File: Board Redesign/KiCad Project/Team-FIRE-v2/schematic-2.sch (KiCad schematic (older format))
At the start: 20 parts, among them J3 USB_B_Mini, J4 Conn_01x03, J5 Conn_ARM_JTAG_SWD_10, U4 TXB0108DQSR, U7 TXB0104RUT

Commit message: Fix: connection of IO-RI
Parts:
- renumbered D2 to D?, D3 to D?, D4 to D?, D5 to D?, J5 to J?, J3 to J?, R11 to R?, R13 to R?, R15 to R?, R16 to R?
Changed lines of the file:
@@
 uC Support
 $Comp
-L Connector:Conn_ARM_JTAG_SWD_10 J5
+L Connector:Conn_ARM_JTAG_SWD_10 J?
 U 1 1 5E6DB242
 P 6220 3020
@@
 $EndComp
 $Comp
-L power:+3.3V #PWR0125
+L power:+3.3V #PWR?
 U 1 1 5E6DD1DD
 P 6970 2770
@@
 	6970 3020 6820 3020
 $Comp
-L power:GND #PWR0126
+L power:GND #PWR?
 U 1 1 5E6E026F
 P 5520 3270
@@
 Keep reset button?
 $Comp
-L Connector:USB_B_Mini J3
+L Connector:USB_B_Mini J?
 U 1 1 5E6EF352
 P 4470 2920
@@
 $EndComp
 $Comp
-L power:GND #PWR0127
+L power:GND #PWR?
 U 1 1 5E6F0DA3
 P 4370 3570
@@
 	5070 3020 4770 3020
 $Comp
-L Device:LED_Small D2
+L Device:LED_Small D?
 U 1 1 5E707545
 P 7670 2920
@@
 $EndComp
 $Comp
-L Device:LED_Small D3
+L Device:LED_Small D?
 U 1 1 5E7081BA
 P 8170 2920
@@
 $EndComp
 $Comp
-L Device:LED_Small D4
+L Device:LED_Small D?
 U 1 1 5E7085D2
 P 8670 3270
@@
 $EndComp
 $Comp
-L Device:LED_Small D5
+L Device:LED_Small D?
 U 1 1 5E709852
 P 9170 3270
@@
 $EndComp
 $Comp
-L power:+3.3V #PWR0128
+L power:+3.3V #PWR?
 U 1 1 5E709BE1
 P 8670 2670
@@
 $EndComp
 $Comp
-L power:+3.3V #PWR0129
+L power:+3.3V #PWR?
 U 1 1 5E70A194
 P 9170 2670
@@
 $EndComp
 $Comp
-L power:GND #PWR0130
+L power:GND #PWR?
 U 1 1 5E70A4EC
 P 7670 2670
@@
 $EndComp
 $Comp
-L power:GND #PWR0131
+L power:GND #PWR?
 U 1 1 5E70B5A5
 P 8170 2670
@@
 $EndComp
 $Comp
-L Device:R R11
+L Device:R R?
 U 1 1 5E70B7B8
 P 7670 3320
@@
 $EndComp
 $Comp
-L Device:R R13
+L Device:R R?
 U 1 1 5E70C353
 P 8170 3320
@@
 $EndComp
 $Comp
-L Device:R R15
+L Device:R R?
 U 1 1 5E7177B2
 P 8670 2920
@@
 $EndComp
 $Comp
-L Device:R R16
+L Device:R R?
 U 1 1 5E717AD1
 P 9170 2920

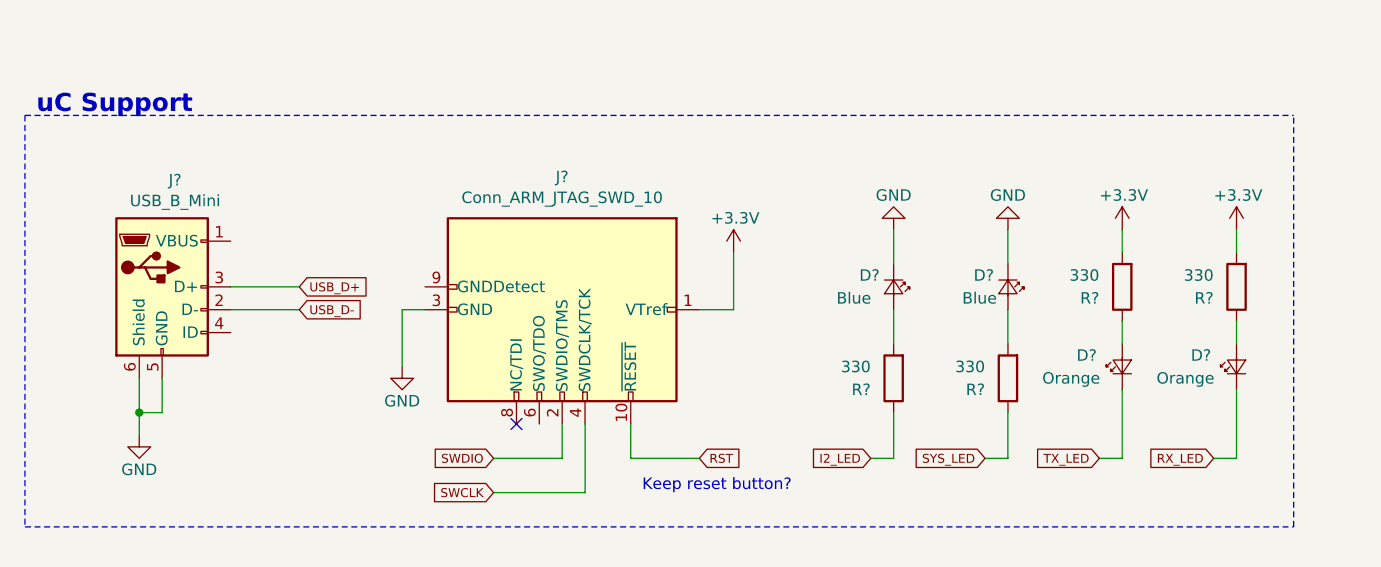
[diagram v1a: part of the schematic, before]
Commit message: Starting complete BOM generation
- Finished schematic(s)
- Started BOM information assignment for final BOM sent to NASA
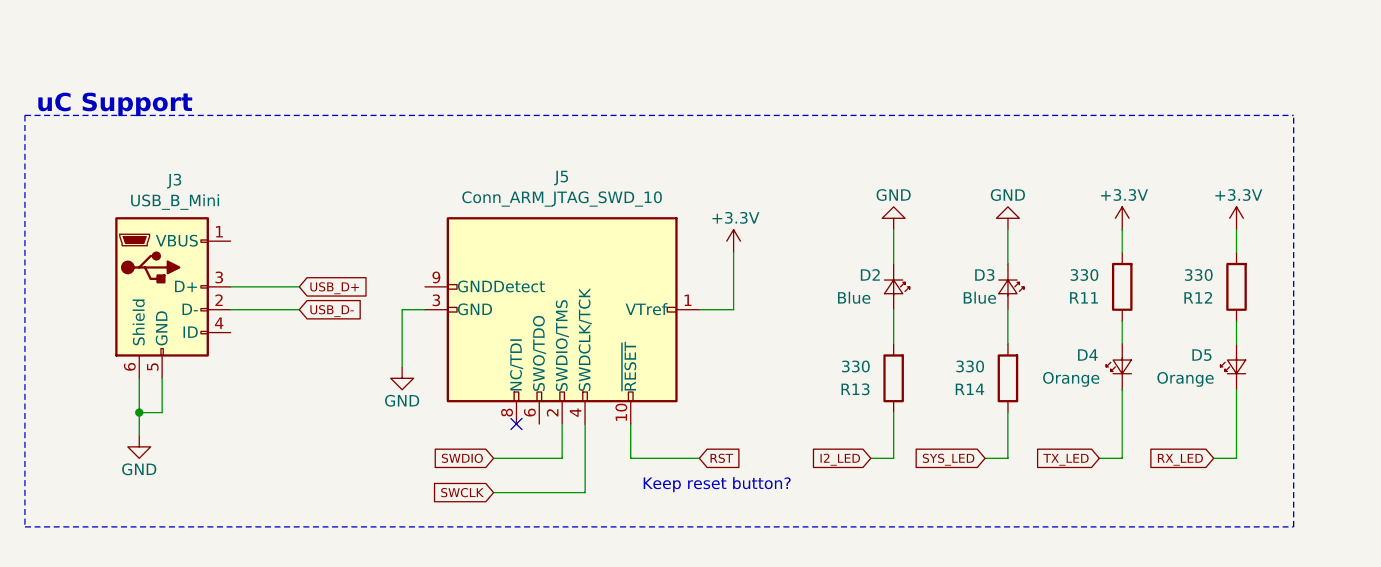
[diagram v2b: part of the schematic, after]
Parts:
- gave numbers to parts that had none: 10
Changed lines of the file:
@@
 EESchema Schematic File Version 4
+LIBS:Team-FIRE-v2-cache
 EELAYER 30 0
 EELAYER END
@@
 Text Notes 3920 2170 0    79   ~ 16
 uC Support
-$Comp
-L Connector:Conn_ARM_JTAG_SWD_10 J?
-U 1 1 5E6DB242
-P 6220 3020
-F 0 "J?" V 5639 3020 50  0000 C CNN
-F 1 "Conn_ARM_JTAG_SWD_10" V 5730 3020 50  0000 C CNN
-F 2 "" H 6220 3020 50  0001 C CNN
-F 3 "http://infocenter.arm.com/help/topic/com.arm.doc.ddi0314h/DDI0314H_coresight_components_trm.pdf" V 5870 1770 50  0001 C CNN
-	1    6220 3020
-	0    1    1    0
-$EndComp
-$Comp
-L power:+3.3V #PWR?
-U 1 1 5E6DD1DD
-P 6970 2770
-F 0 "#PWR?" H 6970 2620 50  0001 C CNN
-F 1 "+3.3V" H 6870 2920 50  0000 L CNN
-F 2 "" H 6970 2770 50  0001 C CNN
-F 3 "" H 6970 2770 50  0001 C CNN
-	1    6970 2770
-	1    0    0    -1
-$EndComp
-Wire Wire Line
-	6970 2770 6970 3020
-Wire Wire Line
-	6970 3020 6820 3020
-$Comp
-L power:GND #PWR?
-U 1 1 5E6E026F
-P 5520 3270
-F 0 "#PWR?" H 5520 3020 50  0001 C CNN
-F 1 "GND" H 5520 3120 50  0000 C CNN
-F 2 "" H 5520 3270 50  0001 C CNN
-F 3 "" H 5520 3270 50  0001 C CNN
-	1    5520 3270
-	1    0    0    -1
-$EndComp
-Wire Wire Line
-	5620 3020 5520 3020
-Wire Wire Line
-	5520 3020 5520 3270
 Text GLabel 5920 3670 0    39   Input ~ 0
 SWDIO
@@
 Keep reset button?
 $Comp
-L Connector:USB_B_Mini J?
+L Connector:USB_B_Mini J3
 U 1 1 5E6EF352
 P 4470 2920
-F 0 "J?" H 4527 3387 50  0000 C CNN
+F 0 "J3" H 4527 3387 50  0000 C CNN
 F 1 "USB_B_Mini" H 4527 3296 50  0000 C CNN
 F 2 "" H 4620 2870 50  0001 C CNN
@@
 $EndComp
 $Comp
-L power:GND #PWR?
+L power:GND #PWR0127
 U 1 1 5E6F0DA3
 P 4370 3570
-F 0 "#PWR?" H 4370 3320 50  0001 C CNN
+F 0 "#PWR0127" H 4370 3320 50  0001 C CNN
 F 1 "GND" H 4370 3420 50  0000 C CNN
 F 2 "" H 4370 3570 50  0001 C CNN
@@
 	5070 3020 4770 3020
 $Comp
-L Device:LED_Small D?
+L Device:LED_Small D2
 U 1 1 5E707545
 P 7670 2920
-F 0 "D?" V 7620 2770 50  0000 L CNN
+F 0 "D2" V 7620 2770 50  0000 L CNN
 F 1 "Blue" V 7720 2670 50  0000 L CNN
 F 2 "" V 7670 2920 50  0001 C CNN
@@
 $EndComp
 $Comp
-L Device:LED_Small D?
+L Device:LED_Small D3
 U 1 1 5E7081BA
 P 8170 2920
-F 0 "D?" V 8120 2770 50  0000 L CNN
+F 0 "D3" V 8120 2770 50  0000 L CNN
 F 1 "Blue" V 8220 2720 50  0000 L CNN
 F 2 "" V 8170 2920 50  0001 C CNN
@@
 $EndComp
 $Comp
-L Device:LED_Small D?
+L Device:LED_Small D4
 U 1 1 5E7085D2
 P 8670 3270
-F 0 "D?" V 8720 3470 50  0000 R CNN
+F 0 "D4" V 8720 3470 50  0000 R CNN
 F 1 "Orange" V 8620 3620 50  0000 R CNN
 F 2 "" V 8670 3270 50  0001 C CNN
@@
 $EndComp
 $Comp
-L Device:LED_Small D?
+L Device:LED_Small D5
 U 1 1 5E709852
 P 9170 3270
-F 0 "D?" V 9220 3470 50  0000 R CNN
+F 0 "D5" V 9220 3470 50  0000 R CNN
 F 1 "Orange" V 9120 3620 50  0000 R CNN
 F 2 "" V 9170 3270 50  0001 C CNN
@@
 $EndComp
 $Comp
-L power:+3.3V #PWR?
+L power:+3.3V #PWR0128
 U 1 1 5E709BE1
 P 8670 2670
-F 0 "#PWR?" H 8670 2520 50  0001 C CNN
+F 0 "#PWR0128" H 8670 2520 50  0001 C CNN
 F 1 "+3.3V" H 8570 2820 50  0000 L CNN
 F 2 "" H 8670 2670 50  0001 C CNN
@@
 $EndComp
 $Comp
-L power:+3.3V #PWR?
+L power:+3.3V #PWR0129
 U 1 1 5E70A194
 P 9170 2670
-F 0 "#PWR?" H 9170 2520 50  0001 C CNN
+F 0 "#PWR0129" H 9170 2520 50  0001 C CNN
 F 1 "+3.3V" H 9070 2820 50  0000 L CNN
 F 2 "" H 9170 2670 50  0001 C CNN
@@
 $EndComp
 $Comp
-L power:GND #PWR?
+L power:GND #PWR0130
 U 1 1 5E70A4EC
 P 7670 2670
-F 0 "#PWR?" H 7670 2420 50  0001 C CNN
+F 0 "#PWR0130" H 7670 2420 50  0001 C CNN
 F 1 "GND" H 7670 2520 50  0000 C CNN
 F 2 "" H 7670 2670 50  0001 C CNN
@@
 $EndComp
 $Comp
-L power:GND #PWR?
+L power:GND #PWR0131
 U 1 1 5E70B5A5
 P 8170 2670
-F 0 "#PWR?" H 8170 2420 50  0001 C CNN
+F 0 "#PWR0131" H 8170 2420 50  0001 C CNN
 F 1 "GND" H 8170 2520 50  0000 C CNN
 F 2 "" H 8170 2670 50  0001 C CNN
@@
 $EndComp
 $Comp
-L Device:R R?
+L Device:R R13
 U 1 1 5E70B7B8
 P 7670 3320
-F 0 "R?" H 7770 3370 50  0000 L CNN
+F 0 "R13" H 7770 3370 50  0000 L CNN
 F 1 "330" H 7770 3270 50  0000 L CNN
 F 2 "Resistor_SMD:R_0603_1608Metric" V 7600 3320 50  0001 C CNN
@@
 $EndComp
 $Comp
-L Device:R R?
+L Device:R R14
 U 1 1 5E70C353
 P 8170 3320
-F 0 "R?" H 8270 3370 50  0000 L CNN
+F 0 "R14" H 8270 3370 50  0000 L CNN
 F 1 "330" H 8270 3270 50  0000 L CNN
 F 2 "Resistor_SMD:R_0603_1608Metric" V 8100 3320 50  0001 C CNN
@@
 $EndComp
 $Comp
-L Device:R R?
+L Device:R R11
 U 1 1 5E7177B2
 P 8670 2920
-F 0 "R?" H 8770 2970 50  0000 L CNN
+F 0 "R11" H 8770 2970 50  0000 L CNN
 F 1 "330" H 8770 2870 50  0000 L CNN
 F 2 "Resistor_SMD:R_0603_1608Metric" V 8600 2920 50  0001 C CNN
@@
 $EndComp
 $Comp
-L Device:R R?
+L Device:R R12
 U 1 1 5E717AD1
 P 9170 2920
-F 0 "R?" H 9270 2970 50  0000 L CNN
+F 0 "R12" H 9270 2970 50  0000 L CNN
 F 1 "330" H 9270 2870 50  0000 L CNN
 F 2 "Resistor_SMD:R_0603_1608Metric" V 9100 2920 50  0001 C CNN
@@
 F1 "SAMD51_IO.sch" 50
 $EndSheet
+Wire Wire Line
+	6970 3020 6820 3020
+Wire Wire Line
+	6970 2770 6970 3020
+$Comp
+L power:+3.3V #PWR0132
+U 1 1 5E6DD1DD
+P 6970 2770
+F 0 "#PWR0132" H 6970 2620 50  0001 C CNN
+F 1 "+3.3V" H 6870 2920 50  0000 L CNN
+F 2 "" H 6970 2770 50  0001 C CNN
+F 3 "" H 6970 2770 50  0001 C CNN
+	1    6970 2770
+	1    0    0    -1
+$EndComp
+$Comp
+L Connector:Conn_ARM_JTAG_SWD_10 J5
+U 1 1 5E6DB242
+P 6220 3020
+F 0 "J5" V 5639 3020 50  0000 C CNN
+F 1 "Conn_ARM_JTAG_SWD_10" V 5730 3020 50  0000 C CNN
+F 2 "" H 6220 3020 50  0001 C CNN
+F 3 "http://infocenter.arm.com/help/topic/com.arm.doc.ddi0314h/DDI0314H_coresight_components_trm.pdf" V 5870 1770 50  0001 C CNN
+	1    6220 3020
+	0    1    1    0
+$EndComp
+Wire Wire Line
+	5520 3020 5520 3270
+Wire Wire Line
+	5620 3020 5520 3020
+$Comp
+L power:GND #PWR0133
+U 1 1 5E6E026F
+P 5520 3270
+F 0 "#PWR0133" H 5520 3020 50  0001 C CNN
+F 1 "GND" H 5520 3120 50  0000 C CNN
+F 2 "" H 5520 3270 50  0001 C CNN
+F 3 "" H 5520 3270 50  0001 C CNN
+	1    5520 3270
+	1    0    0    -1
+$EndComp
 $EndSCHEMATC

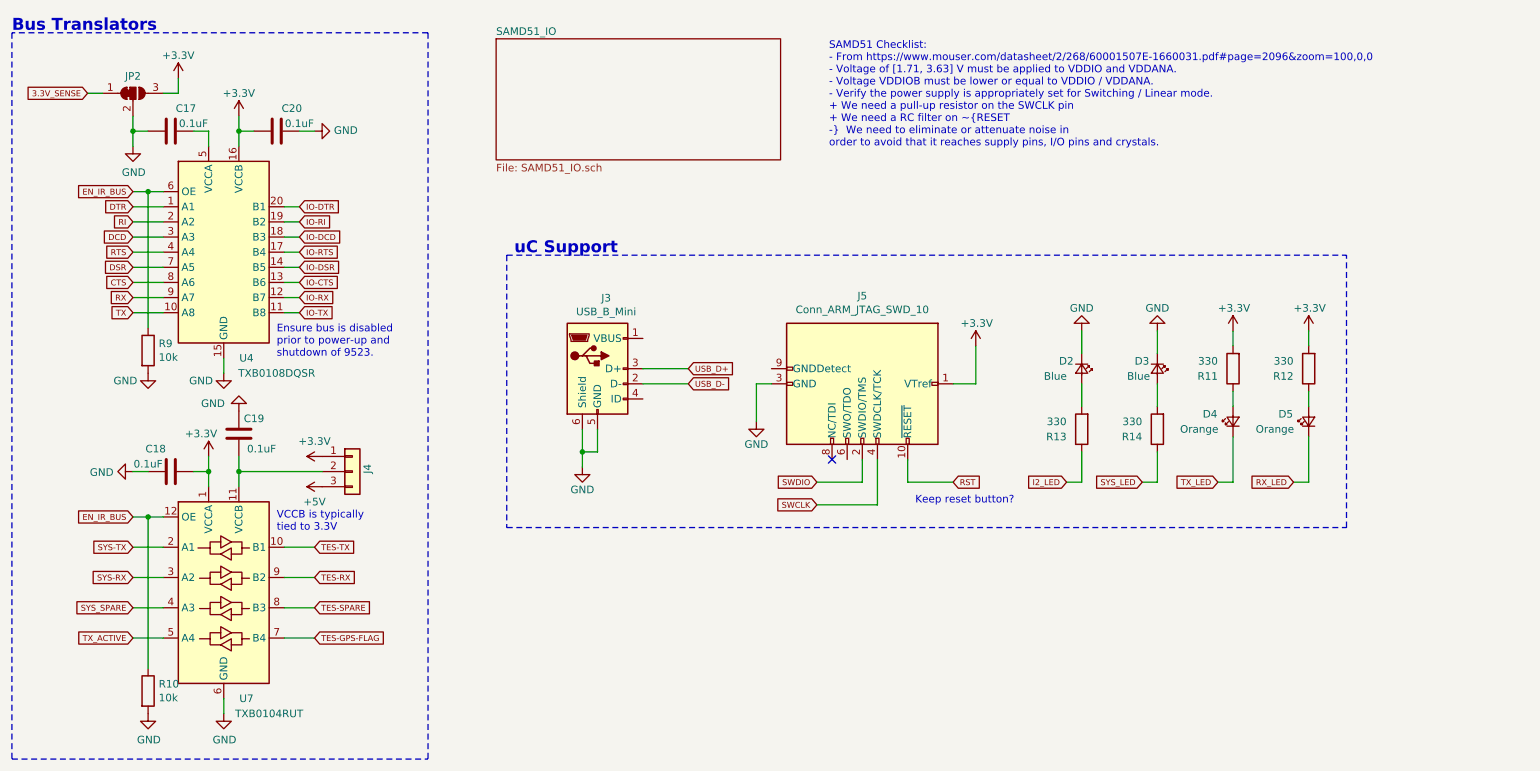
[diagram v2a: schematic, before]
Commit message: Fixed libraries, added BOM info to most components
- Fixed MCP1826T library to be a part of Team-Fire library (not separate)
- Deleted useless library files for various pieces (such as ImportGuides, etc.)
- Fixed inductor value specification for boost converter
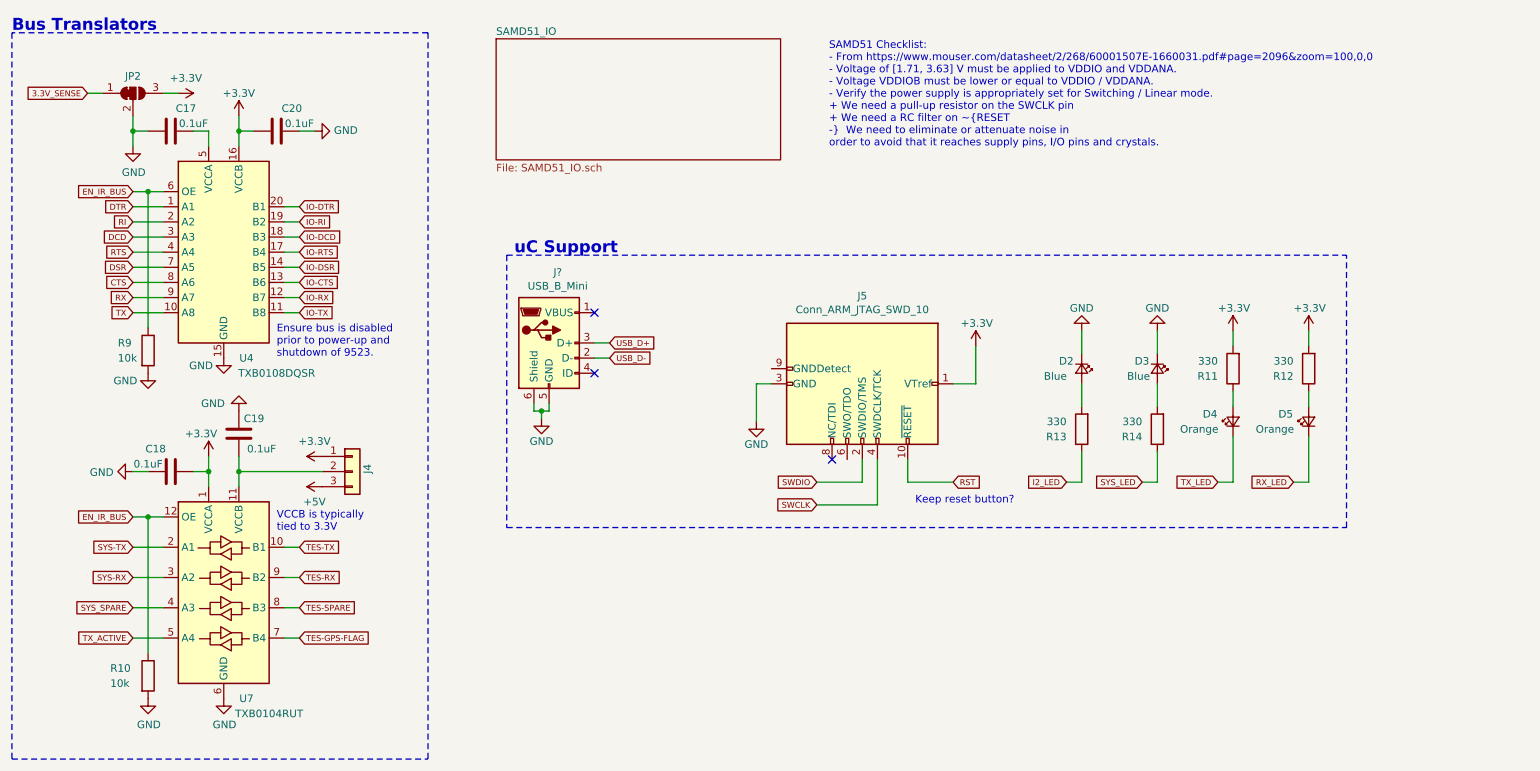
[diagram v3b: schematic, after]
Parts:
- removed J3: USB_B_Mini, symbol Connector:USB_B_Mini
- added J?: USB_B_Mini, symbol Connector:USB_B_Mini
- JP2: footprint (none) -> Jumper:SolderJumper-3_P1.3mm_Bridged2Bar12_RoundedPad1.0x1.5mm
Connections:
- net GND: now also J?.5 (GND), J?.6 (Shield)
- net USB_D+: now also J?.3 (D+)
- net USB_D-: now also J?.2 (D-)
- no-connect marks 1 -> 3
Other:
- moved on the sheet: R10
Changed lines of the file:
@@
 Keep reset button?
-$Comp
-L Connector:USB_B_Mini J3
-U 1 1 5E6EF352
-P 4470 2920
-F 0 "J3" H 4527 3387 50  0000 C CNN
-F 1 "USB_B_Mini" H 4527 3296 50  0000 C CNN
-F 2 "" H 4620 2870 50  0001 C CNN
-F 3 "~" H 4620 2870 50  0001 C CNN
-	1    4470 2920
-	1    0    0    -1
-$EndComp
 $Comp
 L power:GND #PWR0127
 U 1 1 5E6F0DA3
-P 4370 3570
-F 0 "#PWR0127" H 4370 3320 50  0001 C CNN
-F 1 "GND" H 4370 3420 50  0000 C CNN
-F 2 "" H 4370 3570 50  0001 C CNN
-F 3 "" H 4370 3570 50  0001 C CNN
-	1    4370 3570
-	1    0    0    -1
-$EndComp
-Wire Wire Line
-	4370 3320 4370 3470
-Wire Wire Line
-	4370 3470 4470 3470
-Wire Wire Line
-	4470 3470 4470 3320
-Connection ~ 4370 3470
-Wire Wire Line
-	4370 3470 4370 3570
-Text GLabel 5070 2920 2    39   Input ~ 0
+P 4100 3250
+F 0 "#PWR0127" H 4100 3000 50  0001 C CNN
+F 1 "GND" H 4100 3100 50  0000 C CNN
+F 2 "" H 4100 3250 50  0001 C CNN
+F 3 "" H 4100 3250 50  0001 C CNN
+	1    4100 3250
+	1    0    0    -1
+$EndComp
+Text GLabel 4550 2750 2    39   Input ~ 0
 USB_D+
-Text GLabel 5070 3020 2    39   Input ~ 0
+Text GLabel 4550 2850 2    39   Input ~ 0
 USB_D-
-Wire Wire Line
-	5070 2920 4770 2920
-Wire Wire Line
-	5070 3020 4770 3020
 $Comp
 L Device:LED_Small D2
@@
 Text GLabel 1400 4100 0    39   Input ~ 0
 SYS-TX
-Text GLabel 2600 4700 2    39   Input ~ 0
+Text GLabel 2500 4700 2    39   Input ~ 0
 TES-GPS-FLAG
-Text GLabel 2600 4500 2    39   Input ~ 0
+Text GLabel 2500 4500 2    39   Input ~ 0
 TES-SPARE
-Text GLabel 2600 4300 2    39   Input ~ 0
+Text GLabel 2500 4300 2    39   Input ~ 0
 TES-RX
-Text GLabel 2600 4100 2    39   Input ~ 0
+Text GLabel 2500 4100 2    39   Input ~ 0
 TES-TX
-Wire Wire Line
-	2400 4700 2600 4700
-Wire Wire Line
-	2400 4500 2600 4500
-Wire Wire Line
-	2400 4300 2600 4300
-Wire Wire Line
-	2400 4100 2600 4100
 Wire Wire Line
 	1600 4700 1400 4700
@@
 L Device:R R10
 U 1 1 5E55B090
-P 1500 5050
-F 0 "R10" H 1570 5096 50  0000 L CNN
-F 1 "10k" H 1570 5005 50  0000 L CNN
-F 2 "Resistor_SMD:R_0603_1608Metric" V 1430 5050 50  0001 C CNN
-F 3 "~" H 1500 5050 50  0001 C CNN
-	1    1500 5050
+P 1500 4950
+F 0 "R10" H 1250 5000 50  0000 L CNN
+F 1 "10k" H 1250 4900 50  0000 L CNN
+F 2 "Resistor_SMD:R_0603_1608Metric" V 1430 4950 50  0001 C CNN
+F 3 "~" H 1500 4950 50  0001 C CNN
+	1    1500 4950
 	1    0    0    -1
 $EndComp
@@
 L power:GND #PWR0144
 U 1 1 5E554C34
-P 1500 5200
-F 0 "#PWR0144" H 1500 4950 50  0001 C CNN
-F 1 "GND" H 1505 5027 50  0000 C CNN
-F 2 "" H 1500 5200 50  0001 C CNN
-F 3 "" H 1500 5200 50  0001 C CNN
-	1    1500 5200
-	1    0    0    -1
-$EndComp
-Wire Wire Line
-	1500 3900 1500 4900
+P 1500 5100
+F 0 "#PWR0144" H 1500 4850 50  0001 C CNN
+F 1 "GND" H 1505 4927 50  0000 C CNN
+F 2 "" H 1500 5100 50  0001 C CNN
+F 3 "" H 1500 5100 50  0001 C CNN
+	1    1500 5100
+	1    0    0    -1
+$EndComp
+Wire Wire Line
+	1500 3900 1500 4800
 Wire Wire Line
 	1600 3900 1500 3900
@@
 L power:GND #PWR0145
 U 1 1 5E5500F4
-P 2000 5200
-F 0 "#PWR0145" H 2000 4950 50  0001 C CNN
-F 1 "GND" H 2005 5027 50  0000 C CNN
-F 2 "" H 2000 5200 50  0001 C CNN
-F 3 "" H 2000 5200 50  0001 C CNN
-	1    2000 5200
-	1    0    0    -1
-$EndComp
-Wire Wire Line
-	2000 5100 2000 5200
+P 2000 5100
+F 0 "#PWR0145" H 2000 4850 50  0001 C CNN
+F 1 "GND" H 2005 4927 50  0000 C CNN
+F 2 "" H 2000 5100 50  0001 C CNN
+F 3 "" H 2000 5100 50  0001 C CNN
+	1    2000 5100
+	1    0    0    -1
+$EndComp
 $Comp
 L Logic_LevelTranslator:TXB0104RUT U7
@@
 Wire Wire Line
 	1700 1100 1600 1100
-Wire Wire Line
-	1700 1000 1700 1100
 $Comp
 L power:+3.3V #PWR0146
 U 1 1 5E50DD7A
-P 1700 1000
-F 0 "#PWR0146" H 1700 850 50  0001 C CNN
-F 1 "+3.3V" H 1700 1150 50  0000 C CNN
-F 2 "" H 1700 1000 50  0001 C CNN
-F 3 "" H 1700 1000 50  0001 C CNN
-	1    1700 1000
-	1    0    0    -1
+P 1700 1100
+F 0 "#PWR0146" H 1700 950 50  0001 C CNN
+F 1 "+3.3V" V 1600 1150 50  0000 C CNN
+F 2 "" H 1700 1100 50  0001 C CNN
+F 3 "" H 1700 1100 50  0001 C CNN
+	1    1700 1100
+	0    1    1    0
 $EndComp
 $Comp
@@
 F 0 "JP2" H 1400 1213 50  0000 C CNN
 F 1 "SolderJumper_3_Bridged12" H 1400 1214 50  0001 C CNN
-F 2 "" H 1400 1100 50  0001 C CNN
+F 2 "Jumper:SolderJumper-3_P1.3mm_Bridged2Bar12_RoundedPad1.0x1.5mm" H 1400 1100 50  0001 C CNN
 F 3 "~" H 1400 1100 50  0001 C CNN
 	1    1400 1100
@@
 U 1 1 5E5071DF
 P 1500 2800
-F 0 "R9" H 1570 2846 50  0000 L CNN
-F 1 "10k" H 1570 2755 50  0000 L CNN
+F 0 "R9" H 1300 2850 50  0000 L CNN
+F 1 "10k" H 1300 2750 50  0000 L CNN
 F 2 "Resistor_SMD:R_0603_1608Metric" V 1430 2800 50  0001 C CNN
 F 3 "~" H 1500 2800 50  0001 C CNN
@@
 L power:GND #PWR0151
 U 1 1 5E4FE4B4
-P 2000 2950
-F 0 "#PWR0151" H 2000 2700 50  0001 C CNN
-F 1 "GND" H 1850 2900 50  0000 C CNN
-F 2 "" H 2000 2950 50  0001 C CNN
-F 3 "" H 2000 2950 50  0001 C CNN
-	1    2000 2950
-	1    0    0    -1
-$EndComp
-Wire Wire Line
-	2000 2850 2000 2950
+P 2000 2850
+F 0 "#PWR0151" H 2000 2600 50  0001 C CNN
+F 1 "GND" H 1850 2800 50  0000 C CNN
+F 2 "" H 2000 2850 50  0001 C CNN
+F 3 "" H 2000 2850 50  0001 C CNN
+	1    2000 2850
+	1    0    0    -1
+$EndComp
 $Sheet
 S 3800 740  1880 800
@@
 	1    0    0    -1
 $EndComp
+Wire Wire Line
+	2500 4700 2400 4700
+Wire Wire Line
+	2400 4500 2500 4500
+Wire Wire Line
+	2500 4300 2400 4300
+Wire Wire Line
+	2400 4100 2500 4100
+$Comp
+L Connector:USB_B_Mini J?
+U 1 1 5F1B906C
+P 4150 2750
+F 0 "J?" H 4207 3217 50  0000 C CNN
+F 1 "USB_B_Mini" H 4207 3126 50  0000 C CNN
+F 2 "" H 4300 2700 50  0001 C CNN
+F 3 "~" H 4300 2700 50  0001 C CNN
+	1    4150 2750
+	1    0    0    -1
+$EndComp
+Wire Wire Line
+	4050 3150 4050 3200
+Wire Wire Line
+	4050 3200 4100 3200
+Wire Wire Line
+	4150 3200 4150 3150
+Wire Wire Line
+	4100 3200 4100 3250
+Connection ~ 4100 3200
+Wire Wire Line
+	4100 3200 4150 3200
+Wire Wire Line
+	4550 2850 4450 2850
+Wire Wire Line
+	4450 2750 4550 2750
+NoConn ~ 4450 2550
+NoConn ~ 4450 2950
 $EndSCHEMATC
